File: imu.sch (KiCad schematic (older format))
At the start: 2 parts

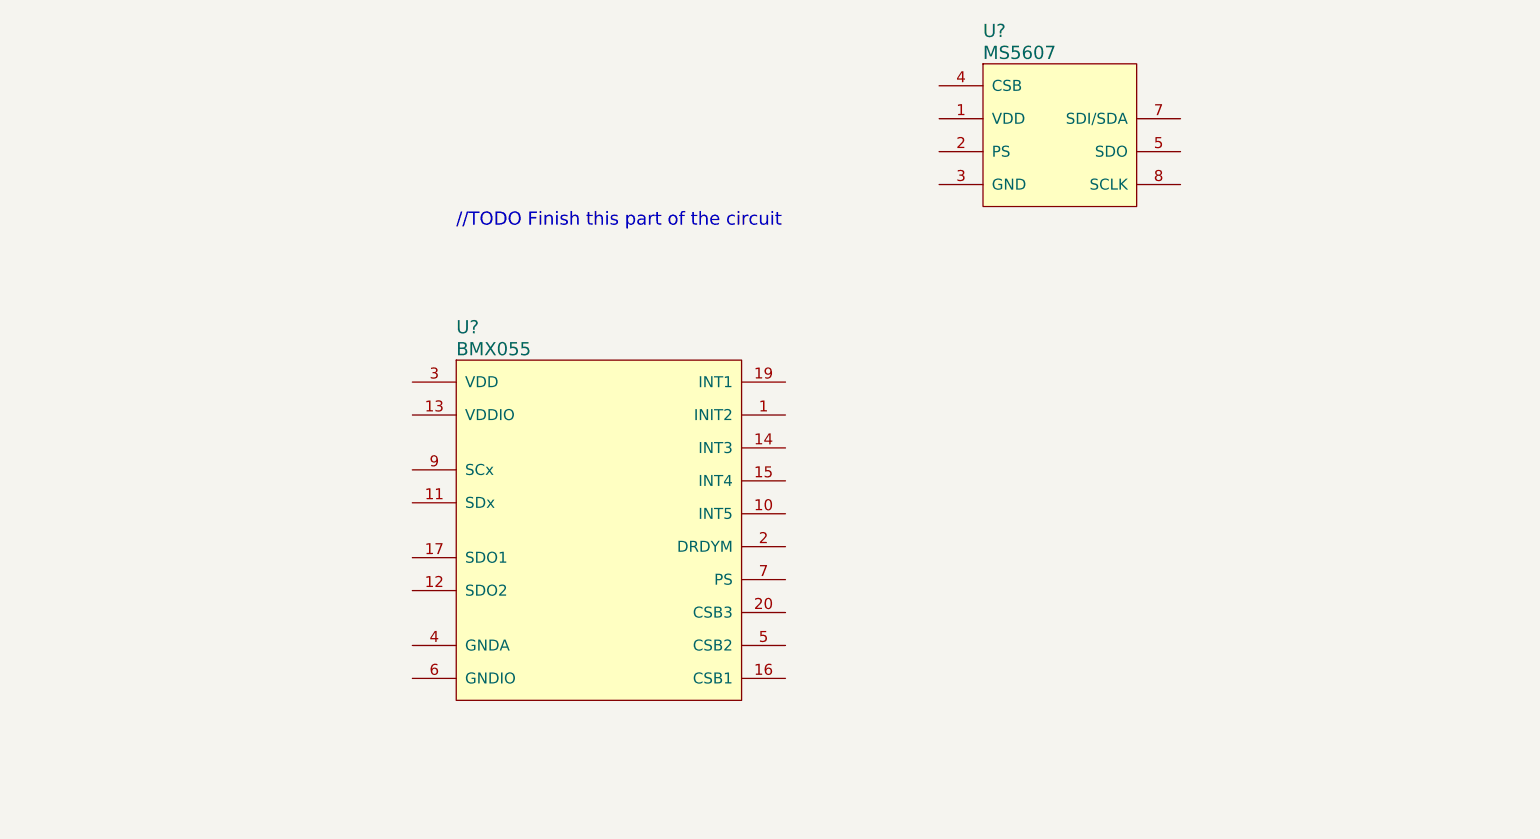
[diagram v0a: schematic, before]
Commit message: added sd card
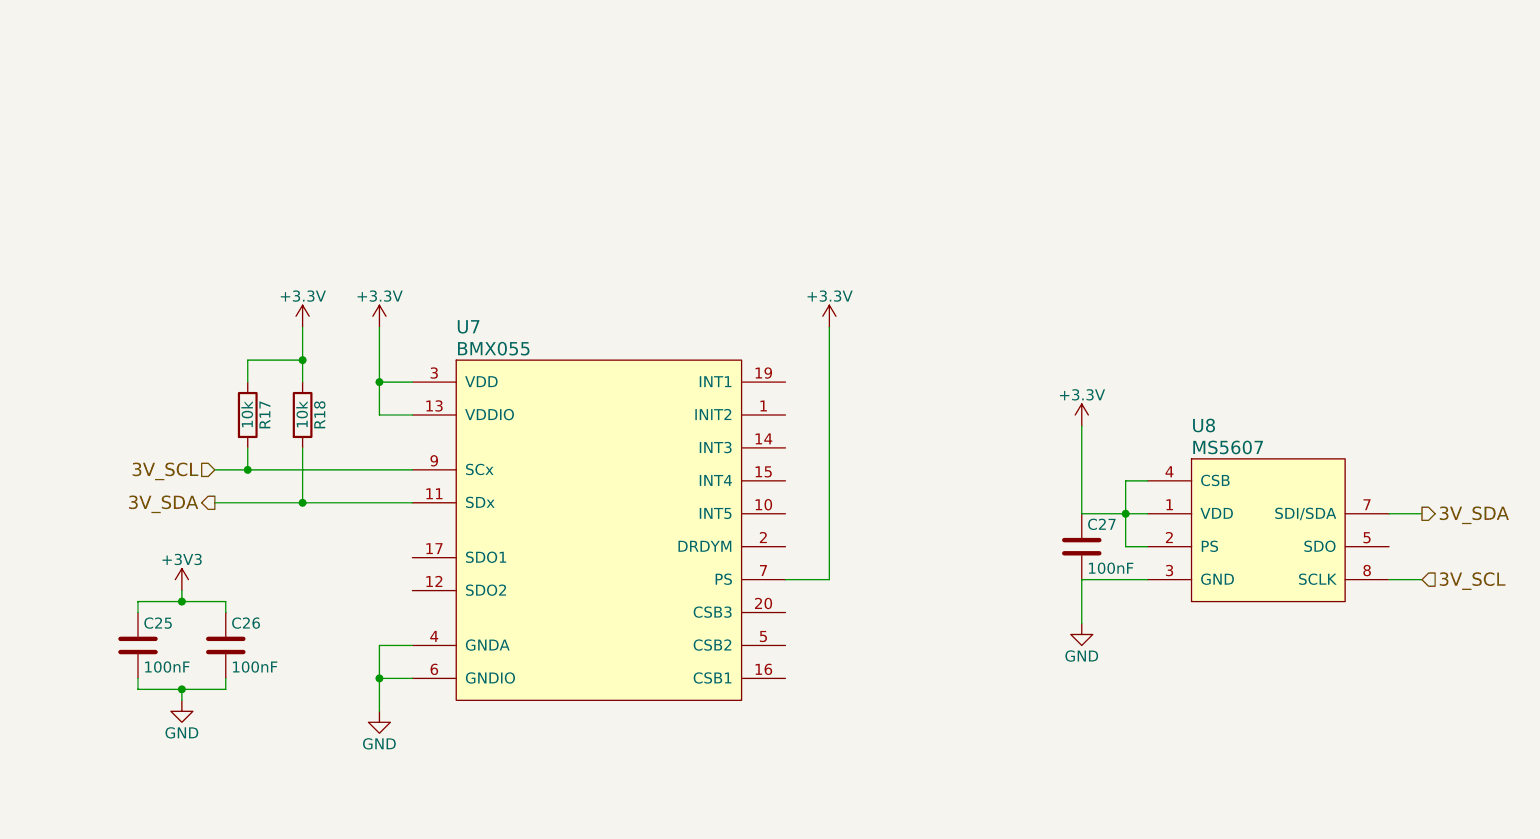
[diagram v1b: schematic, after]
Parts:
- added C25, C26, C27: 100nF, symbol C
- added R17, R18: 10k, symbol R
- gave numbers to parts that had none: 2
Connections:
- net 3V_SDA: now reaches U7.11 (SDx)
- net 3V_SDA: now also U8.7 (SDI/SDA), R18.2
- net +3V3: now reaches U7.13 (VDDIO)
- net +3V3: now also U7.3 (VDD), U7.7 (PS), U8.1 (VDD), U8.2 (PS), U8.4 (CSB), C25.1, C26.1, C27.1, R17.1, R18.1
- net GND: now reaches U7.4 (GNDA)
- net GND: now also U7.6 (GNDIO), U8.3 (GND), C25.2, C26.2, C27.2
- net 3V_SCL: now reaches U7.9 (SCx)
- net 3V_SCL: now also U8.8 (SCLK), R17.2
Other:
- note removed: "//TODO Finish this part of the circuit"
- moved on the sheet: U8

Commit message: Did design review. Changed/confirmed voltage levels
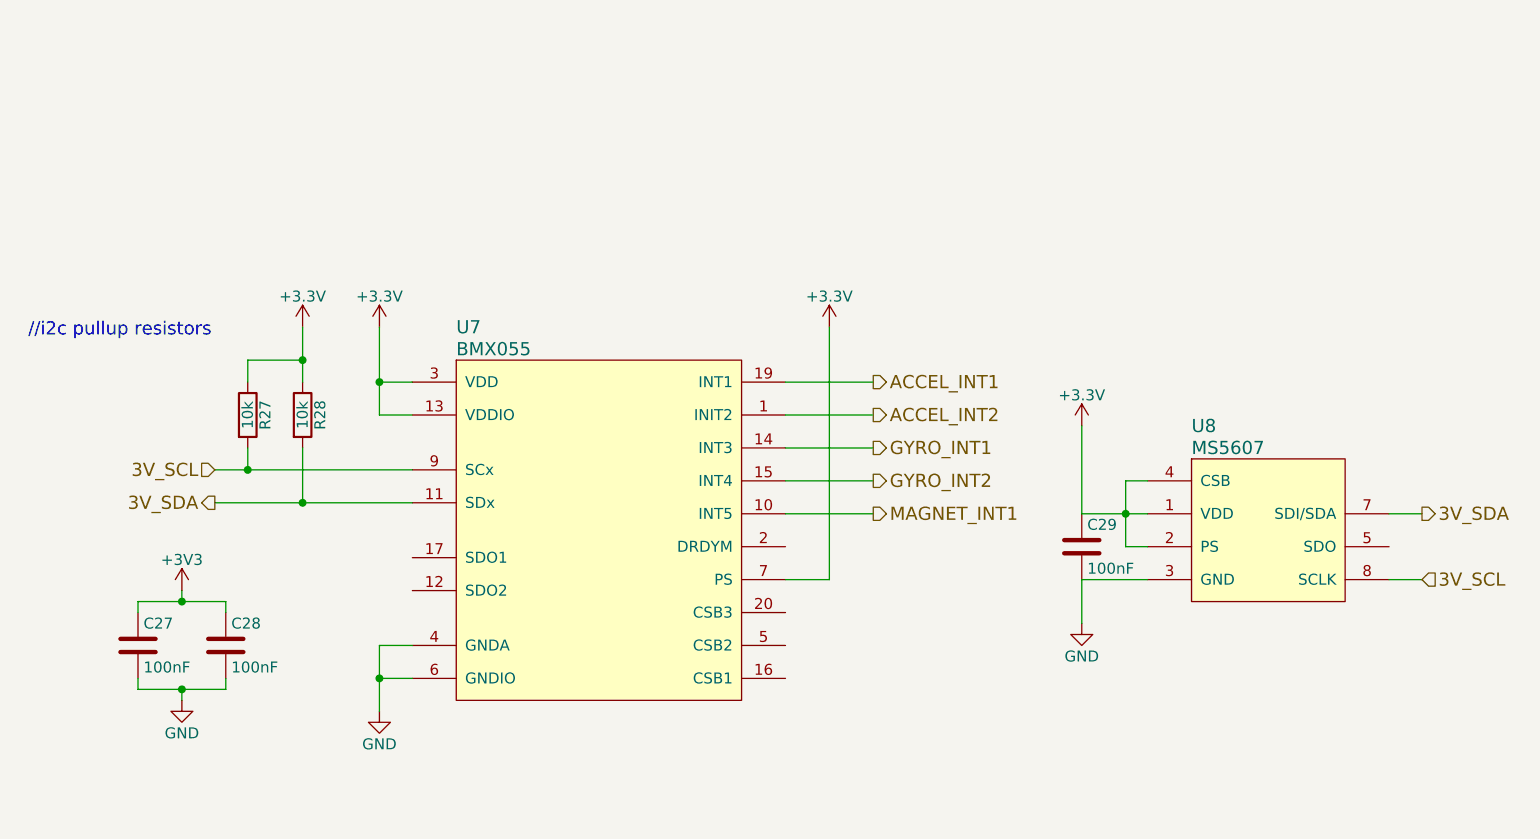
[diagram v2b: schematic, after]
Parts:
- C27: renamed from C25; footprint (none) -> Capacitors_SMD:C_0805
- C28: renamed from C26; footprint (none) -> Capacitors_SMD:C_0805
- C29: renamed from C27; footprint (none) -> Capacitors_SMD:C_0805
- R27: renamed from R17; footprint (none) -> Resistors_SMD:R_0805
- R28: renamed from R18; footprint (none) -> Resistors_SMD:R_0805
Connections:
- net ACCEL_INT2: now reaches U7.1 (INIT2)
- net MAGNET_INT1: now reaches U7.10 (INT5)
- net GYRO_INT1: now reaches U7.14 (INT3)
- net GYRO_INT2: now reaches U7.15 (INT4)
- net ACCEL_INT1: now reaches U7.19 (INT1)
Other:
- note added: "//i2c pullup resistors\n"
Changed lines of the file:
@@
 $EndComp
 $Comp
-L GND #PWR052
+L GND #PWR063
 U 1 1 5A612096
 P 4700 4750
-F 0 "#PWR052" H 4700 4500 50  0001 C CNN
+F 0 "#PWR063" H 4700 4500 50  0001 C CNN
 F 1 "GND" H 4700 4600 50  0000 C CNN
 F 2 "" H 4700 4750 50  0001 C CNN
@@
 $EndComp
 $Comp
-L R R17
+L R R27
 U 1 1 5A61210B
 P 4100 3400
-F 0 "R17" V 4180 3400 50  0000 C CNN
+F 0 "R27" V 4180 3400 50  0000 C CNN
 F 1 "10k" V 4100 3400 50  0000 C CNN
-F 2 "" V 4030 3400 50  0001 C CNN
+F 2 "Resistors_SMD:R_0805" V 4030 3400 50  0001 C CNN
 F 3 "" H 4100 3400 50  0001 C CNN
 	1    4100 3400
@@
 $EndComp
 $Comp
-L R R18
+L R R28
 U 1 1 5A612159
 P 4350 3400
-F 0 "R18" V 4430 3400 50  0000 C CNN
+F 0 "R28" V 4430 3400 50  0000 C CNN
 F 1 "10k" V 4350 3400 50  0000 C CNN
-F 2 "" V 4280 3400 50  0001 C CNN
+F 2 "Resistors_SMD:R_0805" V 4280 3400 50  0001 C CNN
 F 3 "" H 4350 3400 50  0001 C CNN
 	1    4350 3400
@@
 $EndComp
 $Comp
-L C C26
+L C C28
 U 1 1 5A6122A0
 P 4000 4450
-F 0 "C26" H 4025 4550 50  0000 L CNN
+F 0 "C28" H 4025 4550 50  0000 L CNN
 F 1 "100nF" H 4025 4350 50  0000 L CNN
-F 2 "" H 4038 4300 50  0001 C CNN
+F 2 "Capacitors_SMD:C_0805" H 4038 4300 50  0001 C CNN
 F 3 "" H 4000 4450 50  0001 C CNN
 	1    4000 4450
@@
 $EndComp
 $Comp
-L C C25
+L C C27
 U 1 1 5A61245C
 P 3600 4450
-F 0 "C25" H 3625 4550 50  0000 L CNN
+F 0 "C27" H 3625 4550 50  0000 L CNN
 F 1 "100nF" H 3625 4350 50  0000 L CNN
-F 2 "" H 3638 4300 50  0001 C CNN
+F 2 "Capacitors_SMD:C_0805" H 3638 4300 50  0001 C CNN
 F 3 "" H 3600 4450 50  0001 C CNN
 	1    3600 4450
@@
 Connection ~ 3800 4250
 $Comp
-L +3V3 #PWR053
+L +3V3 #PWR064
 U 1 1 5A61255F
 P 3800 4200
-F 0 "#PWR053" H 3800 4050 50  0001 C CNN
+F 0 "#PWR064" H 3800 4050 50  0001 C CNN
 F 1 "+3V3" H 3800 4340 50  0000 C CNN
 F 2 "" H 3800 4200 50  0001 C CNN
@@
 $EndComp
 $Comp
-L GND #PWR054
+L GND #PWR065
 U 1 1 5A61257C
 P 3800 4700
-F 0 "#PWR054" H 3800 4450 50  0001 C CNN
+F 0 "#PWR065" H 3800 4450 50  0001 C CNN
 F 1 "GND" H 3800 4550 50  0000 C CNN
 F 2 "" H 3800 4700 50  0001 C CNN
@@
 	8200 4150 7900 4150
 $Comp
-L C C27
+L C C29
 U 1 1 5A6127D5
 P 7900 4000
-F 0 "C27" H 7925 4100 50  0000 L CNN
+F 0 "C29" H 7925 4100 50  0000 L CNN
 F 1 "100nF" H 7925 3900 50  0000 L CNN
-F 2 "" H 7938 3850 50  0001 C CNN
+F 2 "Capacitors_SMD:C_0805" H 7938 3850 50  0001 C CNN
 F 3 "" H 7900 4000 50  0001 C CNN
 	1    7900 4000
@@
 $EndComp
 Wire Wire Line
-	8200 3850 7900 3850
+	7900 3850 8200 3850
 Wire Wire Line
 	7900 3850 7900 3450
@@
 	8200 3700 8100 3700
 $Comp
-L +3.3V #PWR055
+L +3.3V #PWR066
 U 1 1 5A613111
 P 7900 3450
-F 0 "#PWR055" H 7900 3300 50  0001 C CNN
+F 0 "#PWR066" H 7900 3300 50  0001 C CNN
 F 1 "+3.3V" H 7900 3590 50  0000 C CNN
 F 2 "" H 7900 3450 50  0001 C CNN
@@
 $EndComp
 $Comp
-L GND #PWR056
+L GND #PWR067
 U 1 1 5A613133
 P 7900 4350
-F 0 "#PWR056" H 7900 4100 50  0001 C CNN
+F 0 "#PWR067" H 7900 4100 50  0001 C CNN
 F 1 "GND" H 7900 4200 50  0000 C CNN
 F 2 "" H 7900 4350 50  0001 C CNN
@@
 3V_SCL
 $Comp
-L +3.3V #PWR057
+L +3.3V #PWR068
 U 1 1 5A604203
 P 6750 3000
-F 0 "#PWR057" H 6750 2850 50  0001 C CNN
+F 0 "#PWR068" H 6750 2850 50  0001 C CNN
 F 1 "+3.3V" H 6750 3140 50  0000 C CNN
 F 2 "" H 6750 3000 50  0001 C CNN
@@
 $EndComp
 $Comp
-L +3.3V #PWR058
+L +3.3V #PWR069
 U 1 1 5A604223
 P 4700 3000
-F 0 "#PWR058" H 4700 2850 50  0001 C CNN
+F 0 "#PWR069" H 4700 2850 50  0001 C CNN
 F 1 "+3.3V" H 4700 3140 50  0000 C CNN
 F 2 "" H 4700 3000 50  0001 C CNN
@@
 $EndComp
 $Comp
-L +3.3V #PWR059
+L +3.3V #PWR070
 U 1 1 5A604243
 P 4350 3000
-F 0 "#PWR059" H 4350 2850 50  0001 C CNN
+F 0 "#PWR070" H 4350 2850 50  0001 C CNN
 F 1 "+3.3V" H 4350 3140 50  0000 C CNN
 F 2 "" H 4350 3000 50  0001 C CNN
@@
 	1    0    0    -1
 $EndComp
+Wire Wire Line
+	6550 3250 6950 3250
+Wire Wire Line
+	6550 3400 6950 3400
+Wire Wire Line
+	6550 3550 6950 3550
+Wire Wire Line
+	6550 3700 6950 3700
+Wire Wire Line
+	6550 3850 6950 3850
+Text HLabel 6950 3250 2    60   Output ~ 0
+ACCEL_INT1
+Text HLabel 6950 3400 2    60   Output ~ 0
+ACCEL_INT2
+Text HLabel 6950 3550 2    60   Output ~ 0
+GYRO_INT1
+Text HLabel 6950 3700 2    60   Output ~ 0
+GYRO_INT2
+Text HLabel 6950 3850 2    60   Output ~ 0
+MAGNET_INT1
+Text Notes 3100 3050 0    60   ~ 0
+//i2c pullup resistors\n
 $EndSCHEMATC

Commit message: Started Board layout
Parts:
- U7: footprint (none) -> Current_Control_Systems:BMX055
- U8: footprint (none) -> Current_Control_Systems:MS5607
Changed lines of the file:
@@
 LIBS:TXB0104DR
 LIBS:LOGIC-TXS0108EPWR_TSSOP20_
+LIBS:CurrentControlSystems
 LIBS:Draco-cache
 EELAYER 25 0
@@
 F 0 "U7" H 5050 4600 60  0000 L CNN
 F 1 "BMX055" H 5050 4500 60  0000 L CNN
-F 2 "" H 5850 3450 60  0001 C CNN
+F 2 "Current_Control_Systems:BMX055" H 5850 3450 60  0001 C CNN
 F 3 "" H 5850 3450 60  0001 C CNN
 	1    5700 3800
@@
 F 0 "U8" H 8400 4450 60  0000 L CNN
 F 1 "MS5607" H 8400 4350 60  0000 L CNN
-F 2 "" H 8750 3950 60  0001 C CNN
+F 2 "Current_Control_Systems:MS5607" H 8750 3950 60  0001 C CNN
 F 3 "" H 8750 3950 60  0001 C CNN
 	1    8750 3950
@@
 $EndComp
 $Comp
-L GND #PWR063
+L GND #PWR064
 U 1 1 5A612096
 P 4700 4750
-F 0 "#PWR063" H 4700 4500 50  0001 C CNN
+F 0 "#PWR064" H 4700 4500 50  0001 C CNN
 F 1 "GND" H 4700 4600 50  0000 C CNN
 F 2 "" H 4700 4750 50  0001 C CNN
@@
 Connection ~ 3800 4250
 $Comp
-L +3V3 #PWR064
+L +3V3 #PWR065
 U 1 1 5A61255F
 P 3800 4200
-F 0 "#PWR064" H 3800 4050 50  0001 C CNN
+F 0 "#PWR065" H 3800 4050 50  0001 C CNN
 F 1 "+3V3" H 3800 4340 50  0000 C CNN
 F 2 "" H 3800 4200 50  0001 C CNN
@@
 $EndComp
 $Comp
-L GND #PWR065
+L GND #PWR066
 U 1 1 5A61257C
 P 3800 4700
-F 0 "#PWR065" H 3800 4450 50  0001 C CNN
+F 0 "#PWR066" H 3800 4450 50  0001 C CNN
 F 1 "GND" H 3800 4550 50  0000 C CNN
 F 2 "" H 3800 4700 50  0001 C CNN
@@
 	8200 3700 8100 3700
 $Comp
-L +3.3V #PWR066
+L +3.3V #PWR067
 U 1 1 5A613111
 P 7900 3450
-F 0 "#PWR066" H 7900 3300 50  0001 C CNN
+F 0 "#PWR067" H 7900 3300 50  0001 C CNN
 F 1 "+3.3V" H 7900 3590 50  0000 C CNN
 F 2 "" H 7900 3450 50  0001 C CNN
@@
 $EndComp
 $Comp
-L GND #PWR067
+L GND #PWR068
 U 1 1 5A613133
 P 7900 4350
-F 0 "#PWR067" H 7900 4100 50  0001 C CNN
+F 0 "#PWR068" H 7900 4100 50  0001 C CNN
 F 1 "GND" H 7900 4200 50  0000 C CNN
 F 2 "" H 7900 4350 50  0001 C CNN
@@
 3V_SCL
 $Comp
-L +3.3V #PWR068
+L +3.3V #PWR069
 U 1 1 5A604203
 P 6750 3000
-F 0 "#PWR068" H 6750 2850 50  0001 C CNN
+F 0 "#PWR069" H 6750 2850 50  0001 C CNN
 F 1 "+3.3V" H 6750 3140 50  0000 C CNN
 F 2 "" H 6750 3000 50  0001 C CNN
@@
 $EndComp
 $Comp
-L +3.3V #PWR069
+L +3.3V #PWR070
 U 1 1 5A604223
 P 4700 3000
-F 0 "#PWR069" H 4700 2850 50  0001 C CNN
+F 0 "#PWR070" H 4700 2850 50  0001 C CNN
 F 1 "+3.3V" H 4700 3140 50  0000 C CNN
 F 2 "" H 4700 3000 50  0001 C CNN
@@
 $EndComp
 $Comp
-L +3.3V #PWR070
+L +3.3V #PWR071
 U 1 1 5A604243
 P 4350 3000
-F 0 "#PWR070" H 4350 2850 50  0001 C CNN
+F 0 "#PWR071" H 4350 2850 50  0001 C CNN
 F 1 "+3.3V" H 4350 3140 50  0000 C CNN
 F 2 "" H 4350 3000 50  0001 C CNN

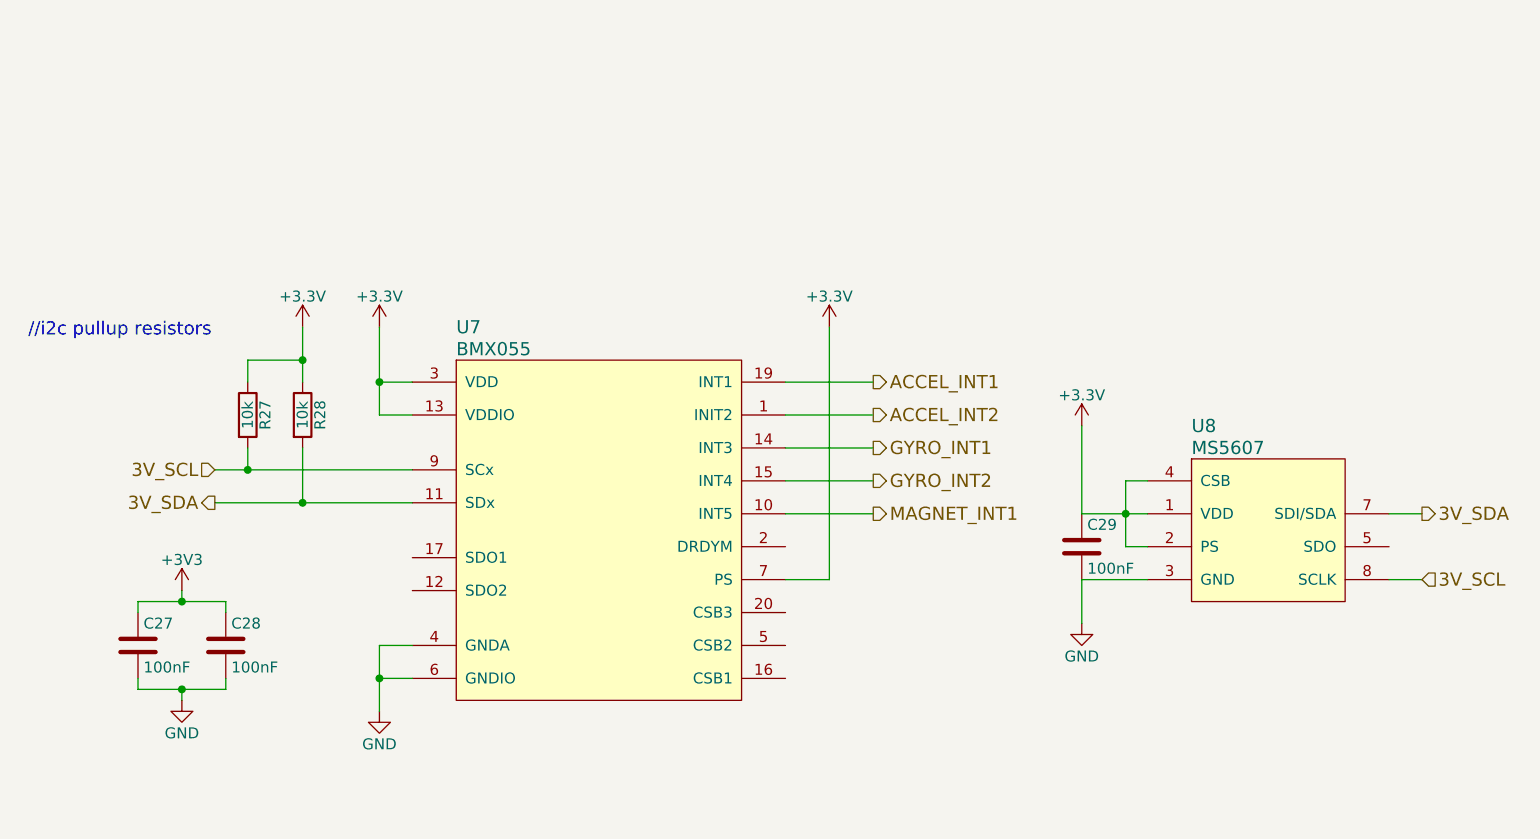
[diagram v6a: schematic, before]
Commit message: Adding bypass capacitors
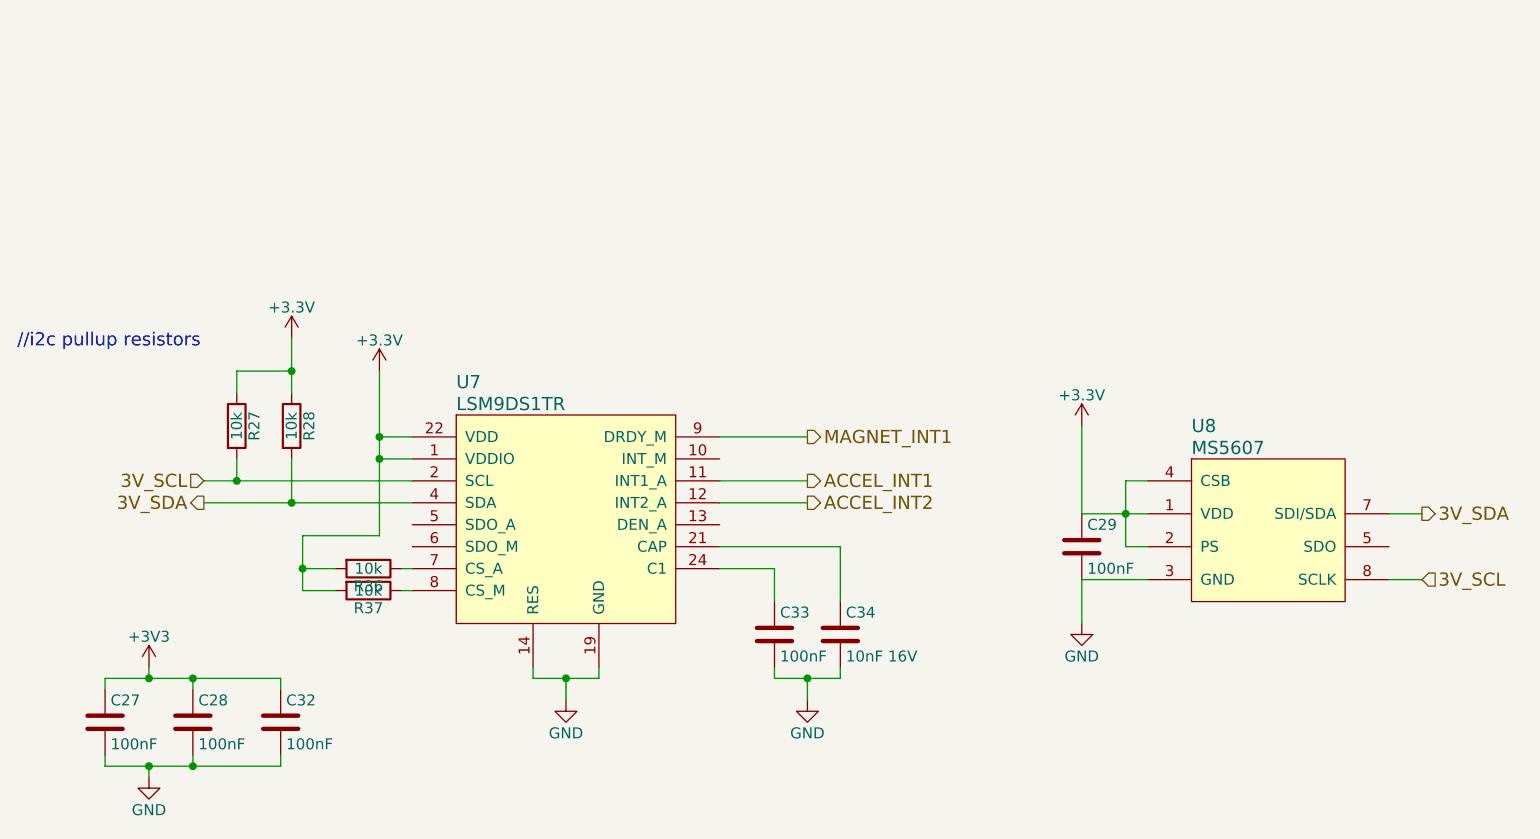
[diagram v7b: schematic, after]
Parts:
- removed U7: BMX055, Current_Control_Systems:BMX055, symbol BMX055
- added C32, C33: 100nF, Capacitors_SMD:C_0805, symbol C
- added C34: 10nF 16V, Capacitors_SMD:C_0805, symbol C
- added R36, R37: 10k, Resistors_SMD:R_0805, symbol R
- added U7: LSM9DS1TR‎, Housings_LGA:LGA-24L_3x3.5mm_Pitch0.43mm, symbol LSM9DS1TR‎
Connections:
- net +3V3: now also C32.1, R36.2, R37.2, U7.1 (VDDIO), U7.22 (VDD), U7.23 (VDD), U7.3 (VDDIO)
- net 3V_SCL: now also U7.2 (SCL)
- net 3V_SDA: now also U7.4 (SDA)
- net ACCEL_INT1: now also U7.11 (INT1_A)
- net ACCEL_INT2: now also U7.12 (INT2_A)
- net GND: now also C32.2, C33.2, C34.2, U7.14 (RES), U7.15 (RES), U7.16 (RES), U7.17 (RES), U7.18 (RES), U7.19 (GND), U7.20 (GND)
- net MAGNET_INT1: now also U7.9 (DRDY_M)
- new net: C34.1, U7.21 (CAP)
- new net: C33.1, U7.24 (C1)
- new net: R36.1, U7.7 (CS_A)
- new net: R37.1, U7.8 (CS_M)
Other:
- moved on the sheet: C27, C28, R27, R28
